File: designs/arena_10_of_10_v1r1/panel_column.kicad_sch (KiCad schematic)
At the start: 4 parts, among them J5 Conn_01x05, J6 Conn_01x05, P1 NA

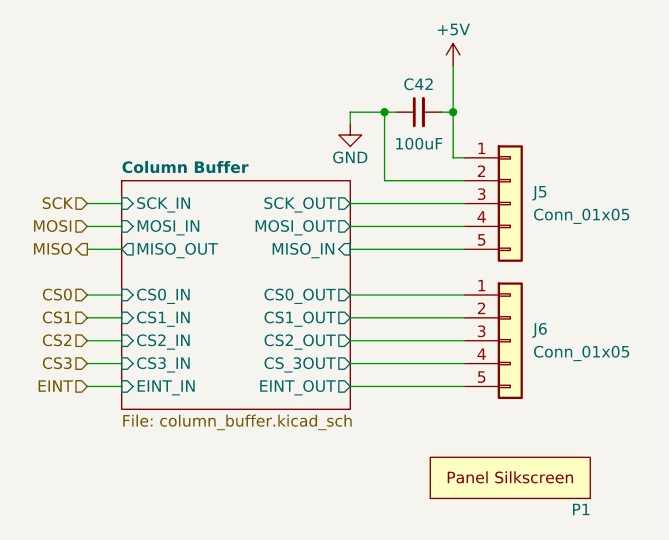
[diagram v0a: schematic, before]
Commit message: Added LCSC part numbers to Symbol Fields Table.
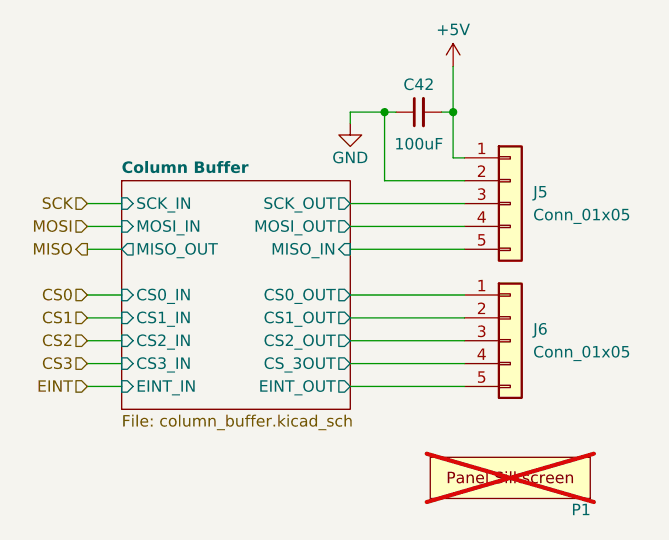
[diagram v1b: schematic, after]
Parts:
- C42: LCSC Part # (none) -> C7432790
- J5, J6: LCSC Part # (none) -> C50950
- P1: now not fitted; now left out of the parts list
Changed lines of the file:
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@@
+			)
+		)
+		(property "LCSC Part #" "C50950"
+			(at 161.29 69.85 0)
+			(effects
+				(font
+					(size 1.27 1.27)
+				)
+				(hide yes)
 			)
 		)
@@
 			)
 		)
+		(property "LCSC Part #" "C7432790"
+			(at 151.13 59.69 90)
+			(effects
+				(font
+					(size 1.27 1.27)
+				)
+				(hide yes)
+			)
+		)
 		(pin "2"
 		)
@@
 		(unit 1)
 		(exclude_from_sim no)
-		(in_bom yes)
+		(in_bom no)
 		(on_board yes)
-		(dnp no)
+		(dnp yes)
 		(property "Reference" "P1"
 			(at 169.164 103.886 0)
@@
 			(at 161.29 85.09 0)
 			(effects
+				(font
+					(size 1.27 1.27)
+				)
+				(hide yes)
+			)
+		)
+		(property "LCSC Part #" "C50950"
+			(at 161.29 85.09 0)
+			(effects

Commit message: Added silkscreens.  Added required FT Rotations/Offsets for JLCPCB.
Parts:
- J5, J6: FT Rotation Offset (none) -> 90
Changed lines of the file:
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@@
+			)
+		)
+		(property "FT Rotation Offset" "90"
+			(at 161.29 69.85 0)
+			(effects
+				(font
+					(size 1.27 1.27)
+				)
+				(hide yes)
 			)
 		)
@@
 			(at 161.29 85.09 0)
 			(effects
+				(font
+					(size 1.27 1.27)
+				)
+				(hide yes)
+			)
+		)
+		(property "FT Rotation Offset" "90"
+			(at 161.29 85.09 0)
+			(effects
